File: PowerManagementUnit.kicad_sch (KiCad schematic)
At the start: 66 parts, among them J1 TYPE-C-31-M-12, U1 SPX3819M5-L-1-8, U2 SPX3819M5-L-1-8, U3 TLV62130RGTR, U4 TLV62130RGTR, U5 LM2776, U6 TLV62130RGTR, U7 TLV62130RGTR

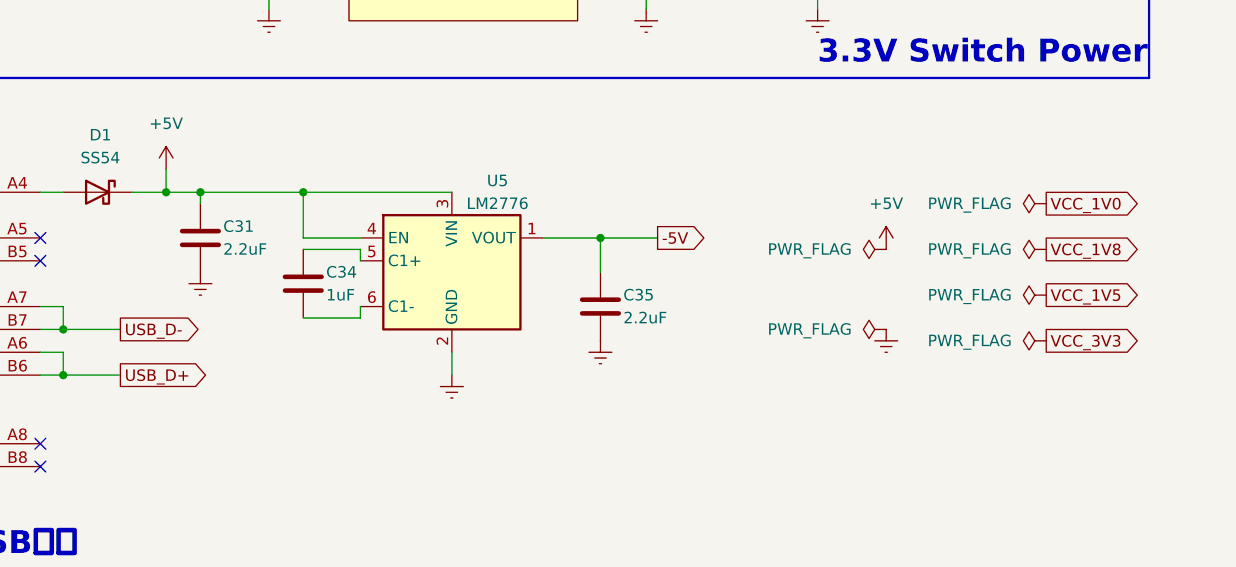
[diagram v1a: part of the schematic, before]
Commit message: 删除-5V电源，添加eMMC模块接口
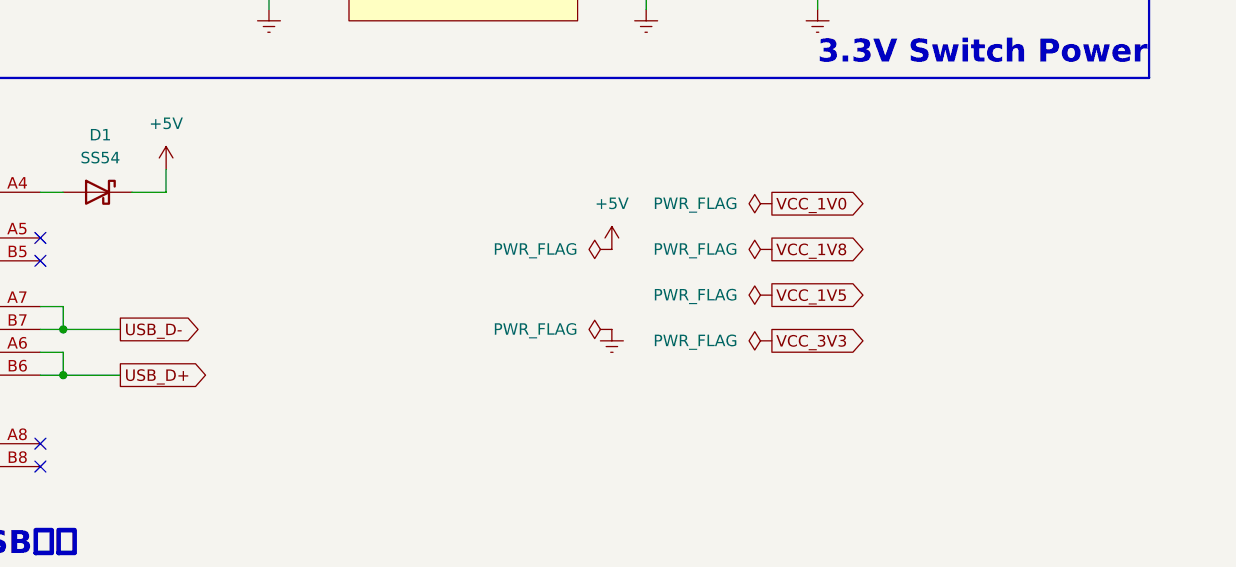
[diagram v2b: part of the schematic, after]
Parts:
- removed C31, C35: 2.2uF, Capacitor_SMD:C_0603_1608Metric, symbol Device:C
- removed C34: 1uF, Capacitor_SMD:C_0402_1005Metric, symbol Device:C
- removed U5: LM2776, Package_TO_SOT_SMD:SOT-23-6, symbol Regulator_SwitchedCapacitor:LM2776
